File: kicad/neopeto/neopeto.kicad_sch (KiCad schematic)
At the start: 26 parts, among them J1 Conn_01x10_Pin, J2 Conn_01x10_Pin, J3 Conn_01x10_Pin, U1 DAC0808_SOIC, U11 CD4066BPW, U12 74HC590, U13 74HC590, U14 K6X4008C1F, U15 74HC4017, U18 74HC00, U19 74HC245, U2 74HC590, U20 74HC245, U21 74HC245, U22 74LS139, U23 74LS139, U24 82C54_PLCC, U3 74HC245, U4 82C55A_PLCC, U5 LM321, U7 74HC245, U8 74HC245

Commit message: wip
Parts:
- removed U1: DAC0808_SOIC, Package_SO:SOIC-16_3.9x9.9mm_P1.27mm, symbol Analog_DAC:DAC0808_SOIC
- removed U11: CD4066BPW, Package_SO:TSSOP-14_4.4x5mm_P0.65mm, symbol Analog_Switch:CD4066BPW
- removed U15: 74HC4017, symbol 4xxx:4017
- removed U20, U3: 74HC245, symbol 74xx:74HC245
- removed U5: LM321, Package_TO_SOT_SMD:SOT-23-5, symbol Amplifier_Operational:LM321
- added C10, C11, C2, C3, C4, C5, C8, C9: 100nF, Capacitor_SMD:C_0603_1608Metric, symbol Device:C
- added C12, C13, C14, C15, C16, C17, C18, C19, C20, C21: 100nF, Capacitor_SMD:C_0402_1005Metric, symbol Device:C
- added C6, C7: 220uF/16V, Capacitor_SMD:CP_Elec_6.3x7.7, symbol Device:C_Polarized
- added H1, H2, H3, H4: MountingHole_Pad, MountingHole:MountingHole_3.2mm_M3_DIN965_Pad, symbol Mechanical:MountingHole_Pad
- added J4: PJ-307, Connector_Audio:Jack_3.5mm_CUI_SJ1-3525N_Horizontal, symbol Connector_Audio:AudioJack3_SwitchTR
- added L1, L2: 1mH, Inductor_THT:L_Radial_D7.2mm_P3.00mm_Murata_1700, symbol Device:L
- added R10, R9: 160, Resistor_SMD:R_0805_2012Metric, symbol Device:R
- added R11, R12: N/C, Resistor_SMD:R_0805_2012Metric, symbol Device:R
- added R13, R14: 0, Resistor_SMD:R_0805_2012Metric, symbol Device:R
- added R15, R16, R4: 470, Resistor_SMD:R_0805_2012Metric, symbol Device:R
- added R5, R6: 150, Capacitor_SMD:C_0603_1608Metric, symbol Device:R
- added R7: 1M, Resistor_SMD:R_0805_2012Metric, symbol Device:R
- added R8: 100K, Resistor_SMD:R_0805_2012Metric, symbol Device:R
- added TP1, TP10, TP11, TP12, TP2, TP3, TP4, TP5, TP6, TP7, TP8, TP9: TestPoint, TestPoint:TestPoint_Pad_D1.5mm, symbol Connector:TestPoint
- added U13, U9: 74HC245, Package_SO:TSSOP-20_4.4x6.5mm_P0.65mm, symbol 74xx:74HC245
- added U17, U18, U19: LM358LV, Package_SO:SOIC-8_3.9x4.9mm_P1.27mm, symbol Amplifier_Operational:OPA1602
- added U21, U22: TLC7258C, Package_SO:SOIC-20W_7.5x12.8mm_P1.27mm, symbol TLC7528C:TLC7528C
- added U23: 74HC4017, Package_SO:SOIC-16_3.9x9.9mm_P1.27mm, symbol 4xxx:4017
- added U24: 74HC86, Package_SO:SO-14_3.9x8.65mm_P1.27mm, symbol 74xx:74HC86
- added U26: 74LVC1G332, Package_TO_SOT_SMD:SOT-23-6, symbol 74xGxx:74LVC1G332
- added X1: ECS-2520MV-12MHZ, Oscillator:Oscillator_SMD_ECS_2520MV-xxx-xx-4Pin_2.5x2.0mm, symbol Oscillator:ECS-2520MV-xxx-xx
- C1: value 0.1uF -> 100nF; footprint (none) -> Capacitor_SMD:C_0603_1608Metric
- J1, J2, J3: footprint (none) -> Connector_PinHeader_2.54mm:PinHeader_1x10_P2.54mm_Vertical
- R1: value 5K -> 10K; footprint (none) -> Resistor_SMD:R_0805_2012Metric
- R2: value 5K -> 15K; footprint (none) -> Resistor_SMD:R_0805_2012Metric
- R3: value 5K -> 470; footprint (none) -> Resistor_SMD:R_0805_2012Metric
- U1: renamed from U18; footprint (none) -> Package_SO:SO-14_3.9x8.65mm_P1.27mm
- U10: renamed from U2; footprint (none) -> Package_SO:SOIC-16_3.9x9.9mm_P1.27mm
- U11: renamed from U12; footprint (none) -> Package_SO:SOIC-16_3.9x9.9mm_P1.27mm
- U12: renamed from U13; footprint (none) -> Package_SO:SOIC-16_3.9x9.9mm_P1.27mm
- U15: renamed from U19; footprint (none) -> Package_SO:TSSOP-20_4.4x6.5mm_P0.65mm
- U16: renamed from U21; footprint (none) -> Package_SO:TSSOP-20_4.4x6.5mm_P0.65mm
- U6: renamed from U22; footprint (none) -> Package_SO:SOIC-16_3.9x9.9mm_P1.27mm
- U6: renamed from U23; footprint (none) -> Package_SO:SOIC-16_3.9x9.9mm_P1.27mm
- U7, U8: footprint (none) -> Package_SO:TSSOP-20_4.4x6.5mm_P0.65mm
- renumbered U24 to U5
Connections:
- net A0 is gone; now on net AB0: J1.9 (Pin_9)
- net A1 is gone; now on net AB1: J1.8 (Pin_8)
- net VA_OUT is gone; now on net +5V: R1.2
- net +5V: now also C1.2, C10.2, C11.2, C12.2, C13.2, C14.2, C15.2, C16.2, C17.2, C18.2, C19.2, C20.2, C21.2, C8.2, C9.2, R7.2, TP7.1, U13.1 (A->B), U13.20 (VCC), U17.8 (V+), U18.8 (V+), U19.8 (V+), U21.17 (VDD), U22.17 (VDD), U23.16 (VDD), U24.14 (VCC), U26.5 (VCC), U9.1 (A->B), U9.20 (VCC), X1.1 (Tri-State), X1.4 (VDD)
- net AB0: now also U21.6 (~{DACA}/DACB)
- net DB0: now also U21.14 (DB0)
- net DB1: now also U21.13 (DB1)
- net DB2: now also U21.12 (DB2)
- net DB3: now also U21.11 (DB3)
- net DB4: now also U21.10 (DB4)
- net DB5: now also U21.9 (DB5)
- net DB6: now also U21.8 (DB6)
- net DB7: now also U21.7 (DB7)
- net GND: now also C1.1, R2.1, C10.1, C11.1, C12.1, C13.1, C14.1, C15.1, C16.1, C17.1, C18.1, C19.1, C2.1, C20.1, C21.1, C3.1, C4.1, C5.1, C8.1, C9.1, H1.1, H2.1, H3.1, H4.1, J4.S, R11.1, R12.1, R8.1, U13.10 (GND), U17.4 (V-), U18.4 (V-), U19.3 (+), U19.4 (V-), U19.5 (+), U21.5 (DGND), U22.15 (~{CS}), U22.5 (DGND), U23.13 (CKEN), U23.8 (VSS), U24.7 (GND), U26.2 (GND), U9.10 (GND), X1.2 (GND); no longer C1.2, R3.2
- net MCLK: now also U22.16 (~{WR}), U23.14 (CLK), X1.3 (OUT)
- net PA0: now also U9.2 (A0); no longer U7.2 (A0)
- net PA1: now also U9.3 (A1); no longer U7.3 (A1)
- net PA2: now also U9.4 (A2); no longer U7.4 (A2)
- net PA3: now also U9.5 (A3); no longer U7.5 (A3)
- net PA4: now also U9.6 (A4); no longer U7.6 (A4)
- net PA5: now also U9.7 (A5); no longer U7.7 (A5)
- net PA6: now also U9.8 (A6); no longer U7.8 (A6)
- net PA7: now also U9.9 (A7); no longer U7.9 (A7)
- net PB0: now also U7.2 (A0), U13.2 (A0); no longer U8.2 (A0)
- net PB1: now also U7.3 (A1), U13.3 (A1); no longer U8.3 (A1)
- net PB2: now also U7.4 (A2), U13.4 (A2); no longer U8.4 (A2)
- net PB3: now also U7.5 (A3), U13.5 (A3); no longer U8.5 (A3)
- net PB4: now also U7.6 (A4), U13.6 (A4); no longer U8.6 (A4)
- net PB5: now also U7.7 (A5), U13.7 (A5); no longer U8.7 (A5)
- net PB6: now also U7.8 (A6), U13.8 (A6); no longer U8.8 (A6)
- net PB7: now also U7.9 (A7), U13.9 (A7); no longer U8.9 (A7)
- net PC0: now also U8.2 (A0)
- net PC1: now also U8.3 (A1)
- net PC2: now also U8.4 (A2)
- net PC3: now also U8.5 (A3)
- net PC4: now also U8.6 (A4)
- net PC5: now also U8.7 (A5)
- net PC6: now also U8.8 (A6)
- net PC7: now also U8.9 (A7)
- net SAMPA10: now also U13.16 (B2), U9.16 (B2)
- net SAMPA11: now also U13.15 (B3), U9.15 (B3)
- net SAMPA12: now also U13.14 (B4), U9.14 (B4)
- net SAMPA13: now also U13.13 (B5), U9.13 (B5)
- net SAMPA14: now also U13.12 (B6), U9.12 (B6)
- net SAMPA15: now also U13.11 (B7), U9.11 (B7)
- net SAMPA8: now also U13.18 (B0), U9.18 (B0)
- net SAMPA9: now also U13.17 (B1), U9.17 (B1)
- net SAMPD0: now also U22.7 (DB7)
- net SAMPD1: now also U22.8 (DB6)
- net SAMPD2: now also U22.9 (DB5)
- net SAMPD3: now also U22.10 (DB4)
- net SAMPD4: now also U22.11 (DB3)
- net SAMPD5: now also U22.12 (DB2)
- net SAMPD6: now also U22.13 (DB1)
- net SAMPD7: now also U22.14 (DB0)
- net VREF: now also R3.2, R4.2, TP1.1, U18.6 (-), U18.7; no longer R2.2
- net ~{CHOP_A}: now also TP11.1, U9.19 (OE); no longer U7.19 (CE)
- net ~{CHOP_B}: now also U7.19 (OE), TP10.1; no longer U8.19 (CE)
- net ~{CHOP_C}: now also U8.19 (OE), TP9.1
- net ~{WRMODE}: now also TP12.1, U13.19 (OE)
- net ~{WR}: now also U21.16 (~{WR})
- net at R1.1: now also R2.2, C2.2, U18.5 (+)
- net at U1.2: now also U24.3
- net at R3.1: now also U21.4 (REFA)
- net at U1.5: now also U24.6
- net at U1.10: now also U24.8
- net ~{CS_MVOL}: now reaches U6.6 (O2)
- net ~{CS_MVOL}: now also U21.15 (~{CS})
- net A2 renamed AB2
- net A3 renamed AB3
- new net: C4.2, L1.2, U17.5 (+)
- new net: R6.2, TP3.1
- new net: TP5.1, U19.1, U21.19 (RFBB), U22.20 (OUTB)
- new net: U19.2 (-), U21.20 (OUTB)
- new net: C7.1, R16.2
- new net: C7.2, J4.R
- new net: R11.2, R13.1, U17.6 (-)
- new net: C3.2, R7.1, R8.2, U18.3 (+)
- new net: R5.1, U22.3 (RFBA)
- new net: R5.2, TP2.1
- new net: R10.1, U22.18 (REFB)
- new net: L2.1, R10.2
- new net: U19.6 (-), U21.2 (OUTA)
- new net: TP4.1, U19.7, U21.3 (RFBA), U22.2 (OUTA)
- new net: L1.1, R9.2
- new net: C5.2, L2.2, U17.3 (+)
- new net: C6.1, R15.2
- new net: C6.2, J4.T
- new net: R13.2, R15.1, U17.7
- new net: R14.2, R16.1, U17.1
- new net: R12.2, R14.1, U17.2 (-)
- new net: R9.1, U22.4 (REFA)
- new net: R6.1, U22.19 (RFBB)
- new net: R4.1, U21.18 (REFB)
- new net CQ0: U23.3 (Q0), U24.1
- new net CQ1: U23.2 (Q1), U24.4
- new net CQ2: U23.4 (Q2), U24.9, U26.6
- new net CQ3: U23.7 (Q3), U24.2
- new net CQ4: U23.10 (Q4), U24.5, U26.1
- new net CQ5: U23.1 (Q5), U24.10, U26.3
- new net CQ6: U23.15 (Reset), U23.5 (Q6)
- new net VGND: TP6.1, U18.1, U18.2 (-), U21.1 (AGND), U22.1 (AGND)
- new net ~{DACA}/DACB: TP8.1, U22.6 (~{DACA}/DACB), U26.4
- no-connect marks 10 -> 26
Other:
- note added: "0.2-1.6V"
- note added: "<3MHz"
- note added: "CHOPPER MODE SAMPLE ADDR MSB ~{WRMODE}=1 ~{SRAM_OE}=0"
- note added: "Fc=16kHz Q=0.625 40dB/dec"
- note added: "L/R sequence generator 0,0,1,0,1,1 ___ left right A B C A B C ABA CBC 2A+B B+2C"
- note added: "WRITE MODE ~{WRMODE}=0 ~{SRAM_OE}=1 ~{SRAM_WE} \ -> SRAM[PB,PA] = PC"
- note added: "http://stades.co.uk/RLC%20filters/RLC%20LPF.html"
- note removed: "10V ?"
- note removed: "3MHz"
- note removed: "CD4066 6MHz @ 5V 74HC4066 30MHz @ 5V"
- note removed: "CHOPPER MODE MSB ~{WRMODE}=1 ~{SRAM_OE}=0"
- note removed: "DIP PINOUT DIFFERS!"
- note removed: "WRITE MODE MSB ~{WRMODE}=0 ~{SRAM_OE}=1 ~{SRAM_WE} \ -> SRAM[PB,PA] = PC"
- moved on the sheet: U10, U11, U12, U14, U1A, U1B, U1C, U1D, U5

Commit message: wip
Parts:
- added C22: 100nF, Capacitor_SMD:C_0603_1608Metric, symbol Device:C
- added C23: 10uF, Capacitor_SMD:C_0805_2012Metric, symbol Device:C
- added C24: 1uF, Capacitor_SMD:C_0603_1608Metric, symbol Device:C
- added D1, D10, D11, D12, D13, D14, D15, D16, D17, D18, D19, D2, D20, D3, D4, D5, D6, D7, D8, D9: LED_Small, LED_SMD:LED_0402_1005Metric, symbol Device:LED_Small
- added D21: BAT54S, Package_TO_SOT_SMD:SOT-23, symbol Diode:BAT54S
- added JP1: SolderJumper_3_Bridged12, Jumper:SolderJumper-3_P1.3mm_Bridged12_RoundedPad1.0x1.5mm_NumberLabels, symbol Jumper:SolderJumper_3_Bridged12
- added R17, R18, R19, R20, R21: 470, Resistor_SMD:R_0805_2012Metric, symbol Device:R
- added R22, R23, R24: 100K, Resistor_SMD:R_0805_2012Metric, symbol Device:R
- added R25: 12K, Resistor_SMD:R_0805_2012Metric, symbol Device:R
- added TP13, TP14, TP15, TP16: TestPoint, TestPoint:TestPoint_Pad_D1.5mm, symbol Connector:TestPoint
- added U2: 74LVC1G00, Package_TO_SOT_SMD:SOT-23-5, symbol 74xGxx:74LVC1G00
- added U20: Pico, MCU_RaspberryPi_and_Boards:RPi_Pico_SMD_TH, symbol MCU_RaspberryPi_and_Boards:Pico
- added U3: CH32V003JxMx, Package_SO:SOP-8_3.9x4.9mm_P1.27mm, symbol MCU_WCH_CH32V0:CH32V003JxMx
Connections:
- net SAMPA16 is gone; now on net GND: U14.2 (A16)
- net SAMPA17 is gone; now on net GND: U14.30 (A17)
- net SAMPA18 is gone; now on net GND: U14.1 (A18)
- net +5V: now also U6.15 (E), C22.1, C23.1, D21.2 (K), R24.2, TP14.1, U2.5 (VCC), U3.4 (VDD)
- net GND: now also U1.12, U1.13, U24.12, U24.13, C22.2, C23.2, D21.1 (A), R25.1, TP15.1, U2.3 (GND), U3.2 (VSS)
- net MCLK: now also JP1.2 (C), TP16.1, U2.1, U2.2; no longer U22.16 (~{WR})
- net S_RIGHT: now reaches C7.2, J4.R
- net S_RIGHT: now also R23.1
- net S_LEFT: now reaches C6.2, J4.T
- net S_LEFT: now also R22.1
- new net: D10.1 (K), D13.1 (K), D14.2 (A), D3.2 (A), D4.1 (K), D5.1 (K), D6.2 (A), D9.2 (A), R19.2
- new net: D1.2 (A), D11.1 (K), D12.2 (A), D17.1 (K), D18.2 (A), D2.1 (K), D3.1 (K), D4.2 (A), R18.2
- new net: D11.2 (A), D12.1 (K), D15.2 (A), D16.1 (K), D5.2 (A), D6.1 (K), D7.1 (K), D8.2 (A), R20.2
- new net: C24.1, R24.1, R25.2
- new net: D13.2 (A), D14.1 (K), D17.2 (A), D18.1 (K), D19.2 (A), D20.1 (K), D7.2 (A), D8.1 (K), R21.2
- new net: C24.2, R22.2, R23.2
- new net: D1.1 (K), D10.2 (A), D15.1 (K), D16.2 (A), D19.1 (K), D2.2 (A), D20.2 (A), D9.1 (K), R17.2
- new net CHX1: R17.1, U3.1 (PD6/PA1)
- new net CHX2: R18.1, TP13.1, U3.8 (PD1/PD4/PD5)
- new net CHX3: R19.1, U3.5 (PC1)
- new net CHX4: R20.1, U3.6 (PC2)
- new net CHX5: R21.1, U3.7 (PC4)
- new net VU: D21.3 (COM), U3.3 (PA2)
- new net ~{DACWR}: JP1.1 (A), U22.16 (~{WR})
- new net ~{MCLK}: JP1.3 (B), U2.4
- no-connect marks 26 -> 22
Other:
- note added: "0.54V"
- moved on the sheet: J4, U24D

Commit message: wip
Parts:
- added D22, D23, D24: LED_Small, LED_SMD:LED_0603_1608Metric, symbol Device:LED_Small
- added J5, J6, J7: Conn_01x10, Connector_PinHeader_2.54mm:PinHeader_1x10_P2.54mm_Vertical, symbol Connector_Generic:Conn_01x10
- added R26, R27, R31, R32: 50, Resistor_SMD:R_0805_2012Metric, symbol Device:R
- added R28, R29, R30: 720, Resistor_SMD:R_0805_2012Metric, symbol Device:R
- added RN1, RN2, RN3, RN4, RN5, RN6: 470, Resistor_SMD:R_Array_Concave_4x0603, symbol Device:R_Pack04
- added U25: 74AUP1G08, Package_TO_SOT_SMD:SOT-353_SC-70-5, symbol 74xGxx:74AUP1G08
- added U27: 74LVC1G332, Package_TO_SOT_SMD:SOT-23-6, symbol 74xGxx:74LVC1G332
- U2: footprint Package_TO_SOT_SMD:SOT-23-5 -> Package_TO_SOT_SMD:SOT-353_SC-70-5
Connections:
- net +5V: now also R28.2, R29.2, R30.2, U25.5 (VCC), U27.5 (VCC)
- net GND: now also R27.1, R32.2, U25.3 (GND), U27.2 (GND)
- net MCLK: now also R31.1, R32.1; no longer X1.3 (OUT)
- net PITCHx256_B: now also U25.2; no longer U11.11 (CPC), U11.13 (CPR)
- net ~{CS_MVOL}: now also D24.1 (K)
- net ~{CS_PP}: now also D22.1 (K)
- net ~{CS_TMR}: now also D23.1 (K)
- net ~{DACA}/DACB: now also R26.1, R27.2; no longer U26.4
- net ~{LOOPEN_B}: now reaches J3.3 (Pin_3)
- net ~{LOOPEN_B}: now also U27.6
- net at U20.1 (GPIO0): now also RN1.1 (R1.1)
- net at U20.10 (GPIO7): now also RN2.4 (R4.1)
- net at U20.11 (GPIO8): now also RN3.1 (R1.1)
- net at U20.12 (GPIO9): now also RN3.2 (R2.1)
- net PI_GND: now reaches U20.13 (GND)
- net PI_GND: now also U20.18 (GND), U20.23 (GND), U20.28 (GND), U20.3 (GND), U20.33 (AGND), U20.38 (GND), U20.8 (GND), J5.10 (Pin_10), J7.1 (Pin_1)
- net at U20.14 (GPIO10): now also RN3.3 (R3.1)
- net at U20.15 (GPIO11): now also RN3.4 (R4.1)
- net at U20.16 (GPIO12): now also RN4.1 (R1.1)
- net at U20.17 (GPIO13): now also RN4.2 (R2.1)
- net at U20.19 (GPIO14): now also RN4.3 (R3.1)
- net at U20.2 (GPIO1): now also RN1.2 (R2.1)
- net at U20.20 (GPIO15): now also RN4.4 (R4.1)
- net at U20.21 (GPIO16): now also RN5.5 (R4.2)
- net at U20.22 (GPIO17): now also RN5.6 (R3.2)
- net at U20.24 (GPIO18): now also RN5.7 (R2.2)
- net at U20.25 (GPIO19): now also RN5.8 (R1.2)
- net at U20.26 (GPIO20): now also RN6.5 (R4.2)
- net at U20.27 (GPIO21): now also RN6.6 (R3.2)
- net at U20.29 (GPIO22): now also RN6.7 (R2.2)
- net at U20.31 (GPIO26_ADC0): now also RN6.8 (R1.2)
- net at U20.4 (GPIO2): now also RN1.3 (R3.1)
- net PI_5V: now reaches U20.40 (VBUS)
- net PI_5V: now also J5.1 (Pin_1), J7.10 (Pin_10)
- net at U20.5 (GPIO3): now also RN1.4 (R4.1)
- net at U20.6 (GPIO4): now also RN2.1 (R1.1)
- net at U20.7 (GPIO5): now also RN2.2 (R2.1)
- net at U20.9 (GPIO6): now also RN2.3 (R3.1)
- net ~{RCO_B}: now reaches U11.9 (~{RCO})
- net ~{RCO_B}: now also U27.1, U27.3
- new net: J7.6 (Pin_6), RN5.1 (R1.1)
- new net: D22.2 (A), R28.1
- new net: J7.2 (Pin_2), RN6.1 (R1.1)
- new net: J7.4 (Pin_4), RN6.3 (R3.1)
- new net: J7.5 (Pin_5), RN6.4 (R4.1)
- new net: R26.2, U26.4
- new net: R31.2, X1.3 (OUT)
- new net: D23.2 (A), R29.1
- new net: U25.1, U27.4
- new net: D24.2 (A), R30.1
- new net PI_AB0: J5.9 (Pin_9), RN3.8 (R1.2)
- new net PI_AB1: J5.8 (Pin_8), RN3.7 (R2.2)
- new net PI_AB2: J5.7 (Pin_7), RN3.6 (R3.2)
- new net PI_AB3: J5.6 (Pin_6), RN3.5 (R4.2)
- new net PI_DB0: J6.9 (Pin_9), RN1.8 (R1.2)
- new net PI_DB1: J6.8 (Pin_8), RN1.7 (R2.2)
- new net PI_DB2: J6.7 (Pin_7), RN1.6 (R3.2)
- new net PI_DB3: J6.6 (Pin_6), RN1.5 (R4.2)
- new net PI_DB4: J6.5 (Pin_5), RN2.8 (R1.2)
- new net PI_DB5: J6.4 (Pin_4), RN2.7 (R2.2)
- new net PI_DB6: J6.3 (Pin_3), RN2.6 (R3.2)
- new net PI_DB7: J6.2 (Pin_2), RN2.5 (R4.2)
- new net Px256_B_GATED: U11.11 (CPC), U11.13 (CPR), U25.4
- new net ~{PI_LOOPEN_B}: J7.3 (Pin_3), RN6.2 (R2.1)
- new net ~{PI_RESET_A}: J7.9 (Pin_9), RN5.4 (R4.1)
- new net ~{PI_RESET_B}: J7.8 (Pin_8), RN5.3 (R3.1)
- new net ~{PI_RESET_C}: J7.7 (Pin_7), RN5.2 (R2.1)
- new net ~{PI_SRAM_OE}: J5.5 (Pin_5), RN4.8 (R1.2)
- new net ~{PI_SRAM_WE}: J5.4 (Pin_4), RN4.7 (R2.2)
- new net ~{PI_WRMODE}: J5.3 (Pin_3), RN4.6 (R3.2)
- new net ~{PI_WR}: J5.2 (Pin_2), RN4.5 (R4.2)
- no-connect marks 22 -> 21
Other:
- moved on the sheet: C10, JP1, TP8, U10, U11, U12, U14

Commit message: before separation
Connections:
- net PI_GPIO16: now reaches RN5.5 (R4.2), U20.21 (GPIO16)
- net PI_GPIO17: now reaches RN5.6 (R3.2), U20.22 (GPIO17)
- net PI_GPIO18: now reaches RN5.7 (R2.2), U20.24 (GPIO18)
- net PI_GPIO19: now reaches RN5.8 (R1.2), U20.25 (GPIO19)
- net PI_GPIO12: now reaches RN4.1 (R1.1), U20.16 (GPIO12)
- net PI_GPIO13: now reaches RN4.2 (R2.1), U20.17 (GPIO13)
- net PI_GPIO14: now reaches RN4.3 (R3.1), U20.19 (GPIO14)
- net PI_GPIO15: now reaches RN4.4 (R4.1), U20.20 (GPIO15)
- net PI_GPIO0: now reaches RN1.1 (R1.1), U20.1 (GPIO0)
- net PI_GPIO7: now reaches RN2.4 (R4.1), U20.10 (GPIO7)
- net PI_GPIO8: now reaches RN3.1 (R1.1), U20.11 (GPIO8)
- net PI_GPIO9: now reaches RN3.2 (R2.1), U20.12 (GPIO9)
- net PI_GPIO10: now reaches RN3.3 (R3.1), U20.14 (GPIO10)
- net PI_GPIO11: now reaches RN3.4 (R4.1), U20.15 (GPIO11)
- net PI_GPIO1: now reaches RN1.2 (R2.1), U20.2 (GPIO1)
- net PI_GPIO20: now reaches RN6.5 (R4.2), U20.26 (GPIO20)
- net PI_GPIO21: now reaches RN6.6 (R3.2), U20.27 (GPIO21)
- net PI_GPIO22: now reaches RN6.7 (R2.2), U20.29 (GPIO22)
- net PI_GPIO26: now reaches RN6.8 (R1.2), U20.31 (GPIO26_ADC0)
- net PI_3V3: now reaches U20.36 (3V3)
- net PI_GPIO2: now reaches RN1.3 (R3.1), U20.4 (GPIO2)
- net PI_GPIO3: now reaches RN1.4 (R4.1), U20.5 (GPIO3)
- net PI_GPIO4: now reaches RN2.1 (R1.1), U20.6 (GPIO4)
- net PI_GPIO5: now reaches RN2.2 (R2.1), U20.7 (GPIO5)
- net PI_GPIO6: now reaches RN2.3 (R3.1), U20.9 (GPIO6)
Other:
- moved on the sheet: J5, J6, J7, RN1, RN2, RN3, RN4, RN5, RN6

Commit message: as ordered
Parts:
- removed J5, J6, J7: Conn_01x10, Connector_PinHeader_2.54mm:PinHeader_1x10_P2.54mm_Vertical, symbol Connector_Generic:Conn_01x10
- removed RN1, RN2, RN3, RN4, RN5, RN6: 470, Resistor_SMD:R_Array_Concave_4x0603, symbol Device:R_Pack04
- removed U20: Pico, MCU_RaspberryPi_and_Boards:RPi_Pico_SMD_TH, symbol MCU_RaspberryPi_and_Boards:Pico
- added C25, C26, C27: 220uF/16V, Capacitor_Tantalum_SMD:CP_EIA-7343-31_Kemet-D, symbol Device:C_Polarized
- added C28, C29, C30, C31: 10uF, Capacitor_SMD:C_0805_2012Metric, symbol Device:C
- added C32: 100nF, Capacitor_SMD:C_0402_1005Metric, symbol Device:C
- added TP17, TP18: TestPoint, TestPoint:TestPoint_Pad_D1.5mm, symbol Connector:TestPoint
- C1, C10, C11, C2, C22, C3, C8, C9: footprint Capacitor_SMD:C_0603_1608Metric -> Capacitor_SMD:C_0402_1005Metric
- C24: footprint Capacitor_SMD:C_0603_1608Metric -> Capacitor_SMD:C_0805_2012Metric
- U6: value 74LS139 -> 74HC139
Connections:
- net +5V: now also C25.1, C26.1, C27.1, C28.2, C29.2, C30.2, C31.2, C32.2
- net GND: now also C25.2, C26.2, C27.2, C28.1, C29.1, C30.1, C31.1, C32.1, TP17.1, TP18.1
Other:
- moved on the sheet: U1D, U24D

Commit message: fixed missing connection to VU on ch32v003
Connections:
- net VU: now also C24.1, R24.1, R25.2
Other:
- moved on the sheet: D1
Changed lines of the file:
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@@
 	)
 	(junction
+		(at 421.64 281.94)
+		(diameter 0)
+		(color 0 0 0 0)
+	)
+	(junction
 		(at 530.86 259.08)
 		(diameter 0)
@@
 	(wire
 		(pts
-			(xy 405.13 281.94) (xy 416.56 281.94)
-		)
-		(stroke
-			(width 0)
-			(type default)
-		)
-	)
-	(wire
-		(pts
 			(xy 167.64 175.26) (xy 167.64 214.63)
 		)
@@
 	(wire
 		(pts
+			(xy 405.13 281.94) (xy 421.64 281.94)
+		)
+		(stroke
+			(width 0)
+			(type default)
+		)
+	)
+	(wire
+		(pts
 			(xy 370.84 62.23) (xy 381 62.23)
 		)
@@
 		(on_board yes)
 		(dnp no)
-		(fields_autoplaced yes)
 		(property "Reference" "U1"
-			(at 107.9417 31.75 0)
+			(at 104.14 27.94 0)
 			(effects
 				(font
@@
 		)
 		(property "Value" "74HC00"
-			(at 107.9417 34.29 0)
+			(at 110.49 33.02 0)
 			(effects
 				(font
@@
 		(on_board yes)
 		(dnp no)
-		(fields_autoplaced yes)
 		(property "Reference" "U24"
-			(at 83.5152 44.45 0)
+			(at 81.28 33.02 0)
 			(effects
 				(font
@@
 					(size 1.27 1.27)
 				)
+				(hide yes)
 			)
 		)
@@
 		(on_board yes)
 		(dnp no)
-		(fields_autoplaced yes)
 		(property "Reference" "U24"
-			(at 83.5152 34.29 0)
+			(at 81.28 30.48 0)
 			(effects
 				(font
@@
 		)
 		(property "Value" "74HC86"
-			(at 83.5152 36.83 0)
+			(at 88.9 35.56 0)
 			(effects
 				(font
@@
 		(on_board yes)
 		(dnp no)
-		(fields_autoplaced yes)
 		(property "Reference" "U24"
-			(at 83.5152 57.15 0)
+			(at 81.28 35.56 0)
 			(effects
 				(font
@@
 					(size 1.27 1.27)
 				)
+				(hide yes)
 			)
 		)
@@
 		(on_board yes)
 		(dnp no)
-		(fields_autoplaced yes)
 		(property "Reference" "U1"
-			(at 107.9417 53.34 0)
+			(at 104.14 33.02 0)
 			(effects
 				(font
@@
 					(size 1.27 1.27)
 				)
+				(hide yes)
 			)
 		)
@@
 	(symbol
 		(lib_id "Device:LED_Small")
-		(at 469.9 241.3 270)
+		(at 469.9 241.3 90)
+		(mirror x)
 		(unit 1)
 		(exclude_from_sim no)
@@
 		(dnp no)
 		(property "Reference" "D1"
-			(at 468.884 236.982 90)
+			(at 470.916 236.982 90)
 			(effects
 				(font
@@
 		)
 		(property "Value" "LED_Small"
-			(at 472.44 242.6334 90)
+			(at 467.36 242.6334 90)
 			(effects
 				(font
@@
 		(on_board yes)
 		(dnp no)
-		(fields_autoplaced yes)
 		(property "Reference" "U1"
-			(at 107.9417 41.91 0)
+			(at 104.14 30.48 0)
 			(effects
 				(font
@@
 					(size 1.27 1.27)
 				)
+				(hide yes)
 			)
 		)

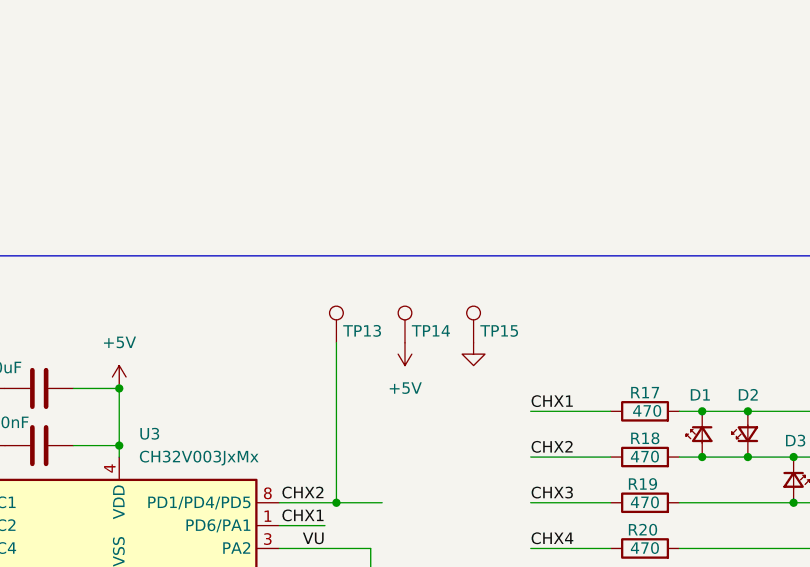
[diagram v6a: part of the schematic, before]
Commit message: layout and schematics for the docs
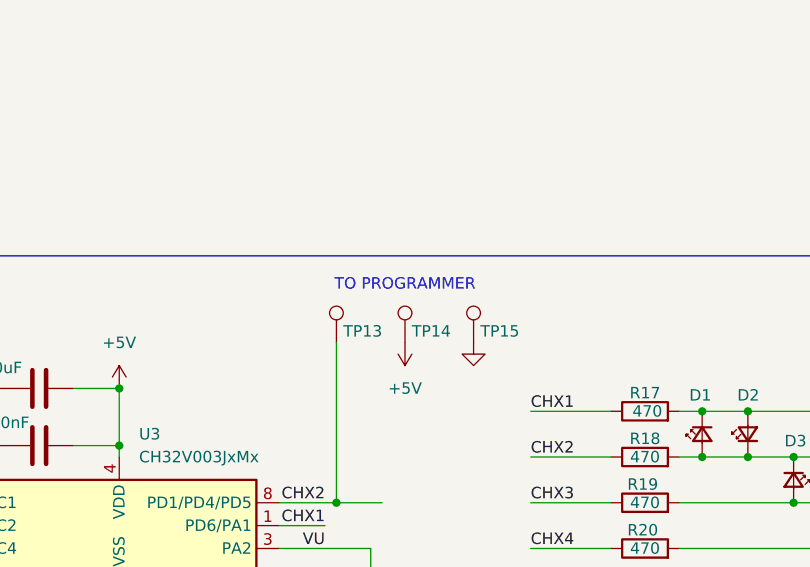
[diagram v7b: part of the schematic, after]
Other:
- note added: "TO PROGRAMMER"
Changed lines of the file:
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@@
+		)
+	)
+	(text "TO PROGRAMMER"
+		(exclude_from_sim no)
+		(at 436.88 224.79 0)
+		(effects
+			(font
+				(size 1.27 1.27)
+			)
 		)
 	)
